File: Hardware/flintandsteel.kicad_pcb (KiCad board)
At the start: 4 copper layers, 57 x 53 mm, 118 parts, among them J1 Conn_01x02_Male, J10 Conn_01x02_Male, J11 Conn_Coaxial, J2 Conn_01x02_Male, J3 Conn_01x02_Male, J4 Conn_01x02_Male, J5 Conn_01x02_Male, J6 Conn_01x02_Male, J7 RBUS, J8 USB_C_Receptacle_USB2.0, J9 Conn_01x02_Male, Q1 MMDT2222A, Q51 PMV20ENR, Q52 PMV20ENR, Q53 PMV20ENR, Q54 PMV20ENR, Q55 PMV20ENR, Q56 PMV20ENR, U1 LTV-247, U2 LTC4411, U3 SC4216H, U4 LTC4411, U5 SN65HVD230, U6 CP2102-GMR-QFN28

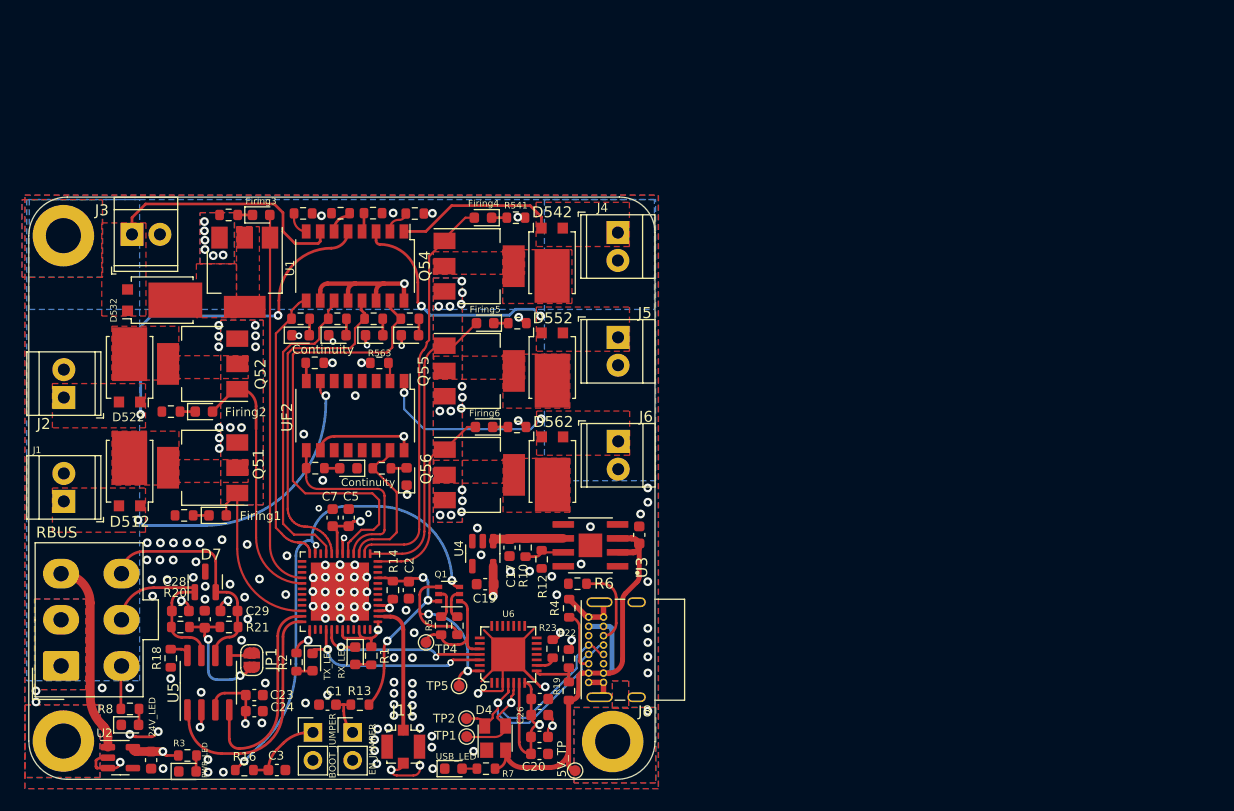
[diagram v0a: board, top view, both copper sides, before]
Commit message: schematic done? + footprints assigned
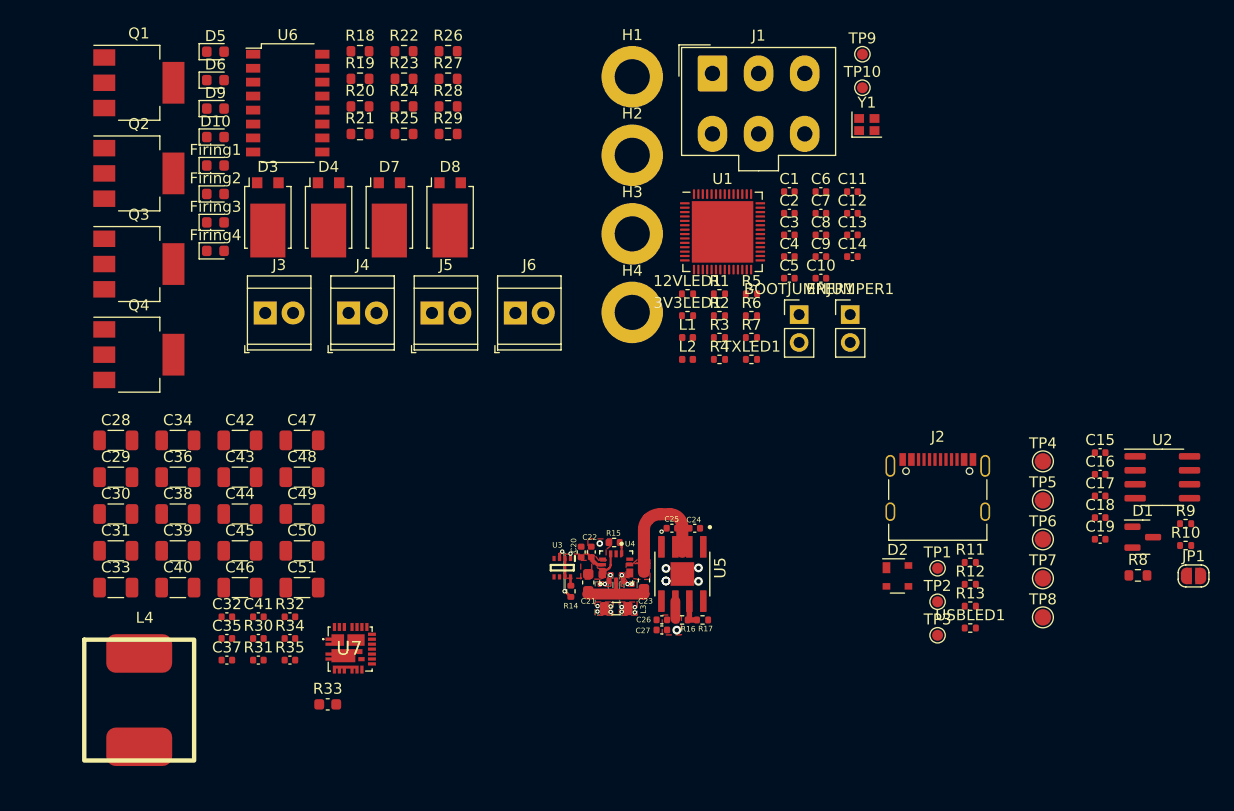
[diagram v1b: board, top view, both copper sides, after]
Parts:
- removed D512, D522, D532, D542, D552, D562: D_Schottky, Package_TO_SOT_SMD:TO-277B
- removed D513, D523, D533, D543, D553, D563: Continuity, LED_SMD:LED_0603_1608Metric
- removed Firing5: D551, LED_SMD:LED_0603_1608Metric
- removed Firing6: D561, LED_SMD:LED_0603_1608Metric
- removed G***: LOGO, iclr:iclr_logo
- removed G***: LOGO, LOGO
- removed GND1: ESP32-PICO-D4, Package_DFN_QFN:QFN-48-1EP_7x7mm_P0.5mm_EP5.3x5.3mm
- removed J10, J9: Conn_01x02_Male, Connector_PinHeader_2.54mm:PinHeader_1x02_P2.54mm_Vertical
- removed J11: Conn_Coaxial, Connector_Coaxial:U.FL_Molex_MCRF_73412-0110_Vertical
- removed J7: RBUS, Connector_Molex:Molex_Mini-Fit_Jr_5566-06A_2x03_P4.20mm_Vertical
- removed J8: USB_C_Receptacle_USB2.0, Connector_USB:USB_C_Receptacle_GCT_USB4085
- removed Q51, Q52, Q53, Q54, Q55, Q56: PMV20ENR, Package_TO_SOT_SMD:SOT-223
- removed R511, R512, R521, R522, R531, R532, R541, R542, R551, R552, R561, R562: 120, Resistor_SMD:R_0603_1608Metric
- removed R513, R523, R533, R543, R553, R563: 10k, Resistor_SMD:R_0603_1608Metric
- removed UF2: LTV-247, Package_SO:SOP-16_4.4x10.4mm_P1.27mm
- added 12VLED1: 12V_LED, Resistor_SMD:R_0402_1005Metric, F.Cu at (178.1, 78.3)
- added 3V3LED1: 3V3LED, Resistor_SMD:R_0402_1005Metric, F.Cu at (178.1, 80.3)
- added BOOTJUMPER1: Conn_01x02_Male, Connector_PinHeader_2.54mm:PinHeader_1x02_P2.54mm_Vertical, F.Cu at (188.3, 80.2)
- added C10: 0.1uF, Capacitor_SMD:C_0402_1005Metric, F.Cu at (190.3, 76.9)
- added C11: 0.1uF, Capacitor_SMD:C_0402_1005Metric, F.Cu at (193.1, 69.0)
- added C12: 4.2pF, Capacitor_SMD:C_0402_1005Metric, F.Cu at (193.1, 71.0)
- added C13: C, Capacitor_SMD:C_0402_1005Metric, F.Cu at (193.1, 72.9)
- added C14: C, Capacitor_SMD:C_0402_1005Metric, F.Cu at (193.1, 74.9)
- added C15: 100nF, Capacitor_SMD:C_0402_1005Metric, F.Cu at (215.7, 92.7)
- added C16: 10uF, Capacitor_SMD:C_0402_1005Metric, F.Cu at (215.7, 94.7)
- added C18: 220pF, Capacitor_SMD:C_0402_1005Metric, F.Cu at (215.7, 98.7)
- added C21: 10uF, Capacitor_SMD:C_0603_1608Metric, F.Cu at (169.1, 104.6)
- added C30: 47uF, Capacitor_SMD:C_1206_3216Metric, F.Cu at (126.1, 98.3)
- added C31: 47uF, Capacitor_SMD:C_1206_3216Metric, F.Cu at (126.1, 101.7)
- added C32: 1uF, Capacitor_SMD:C_0402_1005Metric, F.Cu at (136.2, 107.7)
- added C33: 47uF, Capacitor_SMD:C_1206_3216Metric, F.Cu at (126.1, 105.0)
- added C34: 47uF, Capacitor_SMD:C_1206_3216Metric, F.Cu at (131.7, 91.6)
- added C35: 4.7uF, Capacitor_SMD:C_0402_1005Metric, F.Cu at (136.2, 109.7)
- added C36: 47uF, Capacitor_SMD:C_1206_3216Metric, F.Cu at (131.7, 95.0)
- added C37: 100nF, Capacitor_SMD:C_0402_1005Metric, F.Cu at (136.2, 111.6)
- added C38: 47uF, Capacitor_SMD:C_1206_3216Metric, F.Cu at (131.7, 98.3)
- added C39: 47uF, Capacitor_SMD:C_1206_3216Metric, F.Cu at (131.7, 101.7)
- added C40: 47uF, Capacitor_SMD:C_1206_3216Metric, F.Cu at (131.7, 105.0)
- added C41: 0.1uF, Capacitor_SMD:C_0402_1005Metric, F.Cu at (139.1, 107.7)
- added C42: DNP, Capacitor_SMD:C_1206_3216Metric, F.Cu at (137.4, 91.6)
- added C43: DNP, Capacitor_SMD:C_1206_3216Metric, F.Cu at (137.4, 95.0)
- added C44: DNP, Capacitor_SMD:C_1206_3216Metric, F.Cu at (137.4, 98.3)
- added C45: DNP, Capacitor_SMD:C_1206_3216Metric, F.Cu at (137.4, 101.7)
- added C46: DNP, Capacitor_SMD:C_1206_3216Metric, F.Cu at (137.4, 105.0)
- added C47: DNP, Capacitor_SMD:C_1206_3216Metric, F.Cu at (143.0, 91.6)
- added C48: DNP, Capacitor_SMD:C_1206_3216Metric, F.Cu at (143.0, 95.0)
- added C49: DNP, Capacitor_SMD:C_1206_3216Metric, F.Cu at (143.0, 98.3)
- added C50: DNP, Capacitor_SMD:C_1206_3216Metric, F.Cu at (143.0, 101.7)
- added C51: DNP, Capacitor_SMD:C_1206_3216Metric, F.Cu at (143.0, 105.0)
- added C8: 0.1uF, Capacitor_SMD:C_0402_1005Metric, F.Cu at (190.3, 72.9)
- added C9: 10nF, Capacitor_SMD:C_0402_1005Metric, F.Cu at (190.3, 74.9)
- added D10: Continuity, LED_SMD:LED_0603_1608Metric, F.Cu at (135.2, 64.0)
- added D8: DST1550S, Package_TO_SOT_SMD:TO-277B, F.Cu at (156.5, 71.3)
- added D9: Continuity, LED_SMD:LED_0603_1608Metric, F.Cu at (135.2, 61.4)
- added ENJUMPER1: Conn_01x02_Male, Connector_PinHeader_2.54mm:PinHeader_1x02_P2.54mm_Vertical, F.Cu at (192.9, 80.2)
- added H4: MountingHole_Pad, MountingHole:MountingHole_3.2mm_M3_DIN965_Pad, F.Cu at (173.1, 80.0)
- added L1: 2.0nH, Inductor_SMD:L_0402_1005Metric, F.Cu at (178.1, 82.3)
- added L2: 20nH, Inductor_SMD:L_0402_1005Metric, F.Cu at (178.1, 84.2)
- added L3: 1uH, Inductor_SMD:L_0805_2012Metric, F.Cu at (171.6, 106.9)
- added L4: 680nH, iclr:MGAH1004R68M-10, F.Cu at (123.2, 109.8)
- added Q2: NCV8403, Package_TO_SOT_SMD:SOT-223, F.Cu at (128.2, 67.3)
- added Q3: NCV8403, Package_TO_SOT_SMD:SOT-223, F.Cu at (128.2, 75.6)
- added Q4: NCV8403, Package_TO_SOT_SMD:SOT-223, F.Cu at (128.2, 83.8)
- added R15: 14k, Resistor_SMD:R_0402_1005Metric, F.Cu at (171.4, 100.9)
- added R17: 10k, Resistor_SMD:R_0402_1005Metric, F.Cu at (179.5, 108.0)
- added R24: 120, Resistor_SMD:R_0603_1608Metric, F.Cu at (152.3, 61.2)
- added R25: 120, Resistor_SMD:R_0603_1608Metric, F.Cu at (152.3, 63.7)
- added R26: 120, Resistor_SMD:R_0603_1608Metric, F.Cu at (156.3, 56.2)
- added R27: 120, Resistor_SMD:R_0603_1608Metric, F.Cu at (156.3, 58.7)
- added R28: 10k, Resistor_SMD:R_0603_1608Metric, F.Cu at (156.3, 61.2)
- added R29: 10k, Resistor_SMD:R_0603_1608Metric, F.Cu at (156.3, 63.7)
- added R30: 10k, Capacitor_SMD:C_0402_1005Metric, F.Cu at (139.1, 109.7)
- added R31: 190k, Capacitor_SMD:C_0402_1005Metric, F.Cu at (139.1, 111.6)
- added R32: 10k, Capacitor_SMD:C_0402_1005Metric, F.Cu at (141.9, 107.7)
- added R33: 2.2, Capacitor_SMD:C_0603_1608Metric, F.Cu at (145.4, 115.7)
- added R34: 200k, Capacitor_SMD:C_0402_1005Metric, F.Cu at (141.9, 109.7)
- added R35: 100k, Capacitor_SMD:C_0402_1005Metric, F.Cu at (141.9, 111.6)
- added R9: 60, Resistor_SMD:R_0402_1005Metric, F.Cu at (223.5, 99.2)
- added TP10: TestPoint, TestPoint:TestPoint_Pad_D1.0mm, F.Cu at (194.0, 59.5)
- added TP6: TestPoint, TestPoint:TestPoint_Pad_D1.5mm, F.Cu at (210.5, 100.6)
- added TP7: TestPoint, TestPoint:TestPoint_Pad_D1.5mm, F.Cu at (210.5, 104.2)
- added TP8: TestPoint, TestPoint:TestPoint_Pad_D1.5mm, F.Cu at (210.5, 107.7)
- added TP9: TestPoint, TestPoint:TestPoint_Pad_D1.0mm, F.Cu at (194.0, 56.5)
- added TXLED1: TX_LED, Resistor_SMD:R_0402_1005Metric, F.Cu at (183.9, 84.2)
- added U7: SiC431, iclr:SiC437BEDT1GE3, F.Cu at (147.4, 110.6)
- added USBLED1: USB_LED, Resistor_SMD:R_0402_1005Metric, F.Cu at (203.9, 108.7)
- added Y1: 40MHz±10ppm, Crystal:Crystal_SMD_2016-4Pin_2.0x1.6mm, F.Cu at (194.4, 62.9)
- C1: value 1uF -> 10uF; footprint Capacitor_SMD:C_0603_1608Metric -> Capacitor_SMD:C_0402_1005Metric
- C17: value 10uF -> 47nF; footprint Capacitor_SMD:C_0603_1608Metric -> Capacitor_SMD:C_0402_1005Metric
- C19: value 4.7uF -> 220pF; footprint Capacitor_SMD:C_0603_1608Metric -> Capacitor_SMD:C_0402_1005Metric
- C2, C24, C27: footprint Capacitor_SMD:C_0603_1608Metric -> Capacitor_SMD:C_0402_1005Metric
- C20: value 4.7uF -> 10uF; footprint Capacitor_SMD:C_0603_1608Metric -> Capacitor_SMD:C_0402_1005Metric
- C22: value 1.0uF -> 1uF; footprint Capacitor_SMD:C_0603_1608Metric -> Capacitor_SMD:C_0402_1005Metric
- C23: value 0.1uF -> 22uF
- C25: value 0.1uF -> 4.7uF; footprint Capacitor_SMD:C_0603_1608Metric -> Capacitor_SMD:C_0402_1005Metric
- C26: value 0.1uF -> 10uF; footprint Capacitor_SMD:C_0603_1608Metric -> Capacitor_SMD:C_0402_1005Metric
- C28, C29: value 220pF -> 47uF; footprint Capacitor_SMD:C_0603_1608Metric -> Capacitor_SMD:C_1206_3216Metric
- C3: value 1uF -> 0.1uF; footprint Capacitor_SMD:C_0603_1608Metric -> Capacitor_SMD:C_0402_1005Metric
- C4: value 4.7uF -> 1uF; footprint Capacitor_SMD:C_0603_1608Metric -> Capacitor_SMD:C_0402_1005Metric
- C5, C6: value 10uF -> 0.1uF; footprint Capacitor_SMD:C_0603_1608Metric -> Capacitor_SMD:C_0402_1005Metric
- C7: value 0.1uF -> 1uF; footprint Capacitor_SMD:C_0603_1608Metric -> Capacitor_SMD:C_0402_1005Metric
- D1: value RX_LED -> SM712_SOT23; footprint LED_SMD:LED_0603_1608Metric -> Package_TO_SOT_SMD:SOT-23
- D2: value TX_LED -> SP0503BAHT; footprint LED_SMD:LED_0603_1608Metric -> Package_TO_SOT_SMD:SOT-143
- D3: value PWR_LED -> DST1550S; footprint LED_SMD:LED_0603_1608Metric -> Package_TO_SOT_SMD:TO-277B
- D4: value SP0503BAHT -> DST1550S; footprint Package_TO_SOT_SMD:SOT-143 -> Package_TO_SOT_SMD:TO-277B
- D5: value 24V_LED -> Continuity
- D6: value USB_LED -> Continuity
- D7: value SM712_SOT23 -> DST1550S; footprint Package_TO_SOT_SMD:SOT-23 -> Package_TO_SOT_SMD:TO-277B
- Firing2: value D521 -> D531
- Firing3: value D531 -> D521
- J1: value Conn_01x02_Male -> RBUS; footprint TerminalBlock_TE-Connectivity:TerminalBlock_TE_282834-2_1x02_P2.54mm_Horizontal -> Connector_Molex:Molex_Mini-Fit_Jr_5566-06A_2x03_P4.20mm_Vertical
- J2: value Conn_01x02_Male -> USB_C_Receptacle_USB2.0; footprint TerminalBlock_TE-Connectivity:TerminalBlock_TE_282834-2_1x02_P2.54mm_Horizontal -> Connector_USB:USB_C_Receptacle_Palconn_UTC16-G
- JP1: value SolderJumper_2_Open -> TermJP
- Q1: value MMDT2222A -> NCV8403; footprint Package_TO_SOT_SMD:SOT-363_SC-70-6 -> Package_TO_SOT_SMD:SOT-223
- R1, R3: value 470 -> 10K; footprint Resistor_SMD:R_0603_1608Metric -> Resistor_SMD:R_0402_1005Metric
- R10: value 56k -> 60; footprint Resistor_SMD:R_0603_1608Metric -> Resistor_SMD:R_0402_1005Metric
- R11, R12: value 10K -> 5.1k; footprint Resistor_SMD:R_0603_1608Metric -> Resistor_SMD:R_0402_1005Metric
- R13, R2: footprint Resistor_SMD:R_0603_1608Metric -> Resistor_SMD:R_0402_1005Metric
- R14: value 10K -> 10k; footprint Resistor_SMD:R_0603_1608Metric -> Resistor_SMD:R_0402_1005Metric
- R16: value 470 -> 56k; footprint Resistor_SMD:R_0603_1608Metric -> Resistor_SMD:R_0402_1005Metric
- R18: value 10k -> 120
- R19: value 24k -> 120
- R20, R21: value 60 -> 120
- R22: value 47k -> 10k
- R23: value 4.7k -> 10k
- R4: value 5.1k -> 470; footprint Resistor_SMD:R_0603_1608Metric -> Resistor_SMD:R_0402_1005Metric
- R5: value 10K -> 47.5; footprint Resistor_SMD:R_0603_1608Metric -> Resistor_SMD:R_0402_1005Metric
- R6: value 5.1k -> 499; footprint Resistor_SMD:R_0603_1608Metric -> Resistor_SMD:R_0402_1005Metric
- R7: value 470 -> 3k; footprint Resistor_SMD:R_0603_1608Metric -> Resistor_SMD:R_0402_1005Metric
- R8: value 3k -> 0
- TP4, TP5: footprint TestPoint:TestPoint_Pad_D1.0mm -> TestPoint:TestPoint_Pad_D1.5mm
- U1: value LTV-247 -> ESP32-S3; footprint Package_SO:SOP-16_4.4x10.4mm_P1.27mm -> Package_DFN_QFN:QFN-56-1EP_7x7mm_P0.4mm_EP5.6x5.6mm
- U2: value LTC4411 -> SN65HVD230; footprint Package_TO_SOT_SMD:SOT-23-5 -> Package_SO:SOIC-8_3.9x4.9mm_P1.27mm
- U3: value SC4216H -> LM66200DRLR; footprint iclr:SOIC127P599X175-9N -> iclr:SOTFL50P160X60-8N
- U4: value LTC4411 -> MAX77827AEFD+T; footprint Package_TO_SOT_SMD:SOT-23-5 -> iclr:CONV_MAX77827AEFD+T
- U5: value SN65HVD230 -> SC4215; footprint Package_SO:SOIC-8_3.9x4.9mm_P1.27mm -> iclr:SOIC127P599X175-9N
- U6: value CP2102-GMR-QFN28 -> LTV-247; footprint iclr:QFN28G_0.5-5X5MM -> Package_SO:SOP-16_4.4x10.4mm_P1.27mm
- moved U2 98.2 mm to (221.3, 95.0)
- moved R8 92.6 mm to (219.1, 103.9)
- moved JP1 86.1 mm to (224.2, 104.0), turned to 0 degrees
- moved J2 80.0 mm to (200.9, 95.9), turned to 0 degrees
- moved C4 74.0 mm to (187.4, 74.9), turned to 0 degrees
- moved D1 72.5 mm to (219.6, 100.4), turned to 0 degrees
- moved J1 70.7 mm to (180.4, 58.2), turned to 0 degrees
- moved H3 69.4 mm to (173.1, 72.8)
- moved C3 67.4 mm to (187.4, 72.9)
- moved D6 66.3 mm to (135.2, 58.8)
- moved C1 62.8 mm to (187.4, 69.0), turned to 0 degrees
- moved D5 61.8 mm to (135.2, 56.2)
- moved R3 61.6 mm to (181.0, 82.3), turned to 0 degrees
- moved R10 60.1 mm to (223.5, 101.2), turned to 0 degrees
- moved R19 58.9 mm to (148.3, 58.7), turned to 0 degrees
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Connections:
- C1 pad 1: Net-(C1-Pad1) -> +3V3
- C17 pad 1: GND -> Net-(JP1-B)
- C17 pad 2: Net-(C17-Pad2) -> GND
- C19 pad 1: +3V3 -> GND
- C19 pad 2: GND -> /CAN-
- C2 pad 1: /EN -> /CHIP_PU
- C20 pad 1: GND -> /Power/BBIN
- C20 pad 2: +3V3 -> GND
- C22 pad 1: GND -> /Power/BIAS
- C22 pad 2: +3V3 -> GND
- C23 pad 1: +3V3 -> /Power/BBOUT
- C24 pad 1: +3V3 -> /Power/BBOUT
- C25 pad 1: GND -> /Power/BBOUT
- C25 pad 2: +3V3 -> GND
- C27 pad 1: /Vref -> GND
- C27 pad 2: GND -> +3V3
- C28 pad 1: GND -> /DeployV
- C28 pad 2: /CAN_HIGH -> GND
- C29 pad 1: GND -> /DeployV
- C29 pad 2: /CAN_LOW -> GND
- C3 pad 1: Net-(C3-Pad1) -> /CHIP_PU
- C6 pad 1: GND -> Net-(C6-Pad1)
- C6 pad 2: VBUS -> GND
- D1 pad 1: /RXD -> /CAN-
- D1 pad 2: Net-(D1-Pad2) -> /CAN+
- D2 pad 1: /TXD -> GND
- D2 pad 2: Net-(D2-Pad2) -> VBUS
- D3 pad 1: GND -> Net-(J3-Pin_1)
- D3 pad 2: Net-(D3-Pad2) -> Net-(J3-Pin_1)
- D4 pad 1: GND -> Net-(J4-Pin_1)
- D4 pad 2: VBUS -> Net-(J4-Pin_1)
- D4 pad 3: /Data- -> Net-(D4-K)
- D5 pad 2: Net-(D5-Pad2) -> Net-(D5-A)
- D6 pad 2: Net-(D6-Pad2) -> Net-(D6-A)
- D7 pad 1: /CAN_HIGH -> Net-(J5-Pin_1)
- D7 pad 2: /CAN_LOW -> Net-(J5-Pin_1)
- D7 pad 3: GND -> Net-(D7-K)
- Firing1 pad 1: Net-(Firing1-Pad1) -> Net-(Firing1-K)
- Firing2 pad 1: Net-(R521-Pad1) -> Net-(Firing2-K)
- Firing2 pad 2: /Nuke 2 -> /Nuke 3
- Firing3 pad 2: /Nuke 3 -> /Nuke 2
- J1 pad 1: Net-(D512-Pad1) -> GND
- J1 pad 2: +24V -> GND
- J3 pad 1: Net-(D532-Pad1) -> Net-(J3-Pin_1)
- J3 pad 2: +24V -> +12V
- J4 pad 1: Net-(D542-Pad1) -> Net-(J4-Pin_1)
- J4 pad 2: +24V -> +12V
- J5 pad 1: Net-(D552-Pad1) -> Net-(J5-Pin_1)
- J5 pad 2: +24V -> +12V
- J6 pad 1: Net-(D562-Pad1) -> Net-(J6-Pin_1)
- J6 pad 2: +24V -> +12V
- JP1 pad 1: /Vref -> /CAN-BUS/Vref
- JP1 pad 2: Net-(JP1-Pad2) -> Net-(JP1-B)
- Q1 pad 1: /RTS -> /Nuke 1
- Q1 pad 2: Net-(Q1-Pad2) -> Net-(D3-K)
- Q1 pad 3: /BOOT -> GND
- Q1 pad 4: /DTR -> Net-(D3-K)
- R1 pad 2: Net-(D1-Pad2) -> /CHIP_PU
- R10 pad 1: Net-(C17-Pad2) -> Net-(JP1-B)
- R10 pad 2: Net-(R10-Pad2) -> /CAN-
- R11 pad 1: Net-(Q1-Pad2) -> Net-(J2-CC1)
- R11 pad 2: /DTR -> GND
- R12 pad 1: Net-(R10-Pad2) -> GND
- R12 pad 2: GND -> Net-(J2-CC2)
- R13 pad 1: /EN -> VBUS
- R13 pad 2: Net-(C1-Pad1) -> Net-(USBLED1-A)
- R14 pad 1: +3V3 -> VBUS
- R14 pad 2: /EN -> Net-(U3-ST)
- R16 pad 1: /BOOT -> +3V3
- R16 pad 2: Net-(C3-Pad1) -> /Power/FBIn
- R18 pad 1: Net-(R18-Pad1) -> Net-(Firing1-K)
- R19 pad 1: VBUS -> Net-(Firing2-K)
- R19 pad 2: Net-(R19-Pad2) -> GND
- R2 pad 2: Net-(D2-Pad2) -> Net-(TXLED1-A)
- R20 pad 1: /CAN_HIGH -> /Cont 1
- R20 pad 2: /Vref -> Net-(D5-A)
- R21 pad 1: /Vref -> /Cont 3
- R21 pad 2: /CAN_LOW -> Net-(D6-A)
- R22 pad 1: GND -> Net-(R22-Pad1)
- R22 pad 2: Net-(R19-Pad2) -> GND
- R23 pad 1: +3V3 -> Net-(R23-Pad1)
- R23 pad 2: Net-(R23-Pad2) -> GND
- R3 pad 1: Net-(D3-Pad2) -> +3V3
- R3 pad 2: +3V3 -> /BOOT
- R4 pad 2: GND -> +3V3
- R5 pad 1: Net-(Q1-Pad5) -> GND
- R5 pad 2: /RTS -> Net-(C12-Pad1)
- R6 pad 1: GND -> /TXD
- R6 pad 2: Net-(J8-PadB5) -> Net-(U1-U0TXD/PROG/GPIO43)
- R7 pad 1: VBUS -> +12V
- R7 pad 2: Net-(D6-Pad2) -> Net-(12VLED1-A)
- R8 pad 1: +24V -> Net-(U2-Rs)
- R8 pad 2: Net-(D5-Pad2) -> GND
- TP4 pad 1: /RTS -> /Power/BBIN
- TP5 pad 1: /DTR -> RBUS_uC_V
- U1 pad 1: Net-(D542-Pad1) -> Net-(U1-LNA_IN/RF)
- U1 pad 10: +3V3 -> unconnected-(U1-GPIO5/ADC1_CH4-Pad10)
- U1 pad 11: /Cont 2 -> unconnected-(U1-GPIO6/ADC1_CH5-Pad11)
- U1 pad 12: +3V3 -> unconnected-(U1-GPIO7/ADC1_CH6-Pad12)
- U1 pad 13: /Cont 5 -> unconnected-(U1-GPIO8/ADC1_CH7-Pad13)
- U1 pad 14: +3V3 -> unconnected-(U1-GPIO9/ADC1_CH8-Pad14)
- U1 pad 15: /Cont 4 -> unconnected-(U1-GPIO10/ADC1_CH9-Pad15)
- U1 pad 16: +3V3 -> unconnected-(U1-GPIO11/ADC2_CH0-Pad16)
- U1 pad 2: Net-(R543-Pad1) -> Net-(C6-Pad1)
- U1 pad 3: Net-(D552-Pad1) -> Net-(C6-Pad1)
- U1 pad 4: Net-(R553-Pad1) -> /CHIP_PU
- U1 pad 5: Net-(D522-Pad1) -> /BOOT
- U1 pad 6: Net-(R523-Pad1) -> unconnected-(U1-GPIO1/ADC1_CH0-Pad6)
- U1 pad 7: Net-(D532-Pad1) -> unconnected-(U1-GPIO2/ADC1_CH1-Pad7)
- U1 pad 8: Net-(R533-Pad1) -> unconnected-(U1-GPIO3/ADC1_CH2-Pad8)
- U1 pad 9: /Cont 3 -> unconnected-(U1-GPIO4/ADC1_CH3-Pad9)
- U2 pad 1: Net-(J7-Pad3) -> /CAN_TX
- U2 pad 3: GND -> +3V3
- U2 pad 4: unconnected-(U2-Pad4) -> /CAN_RX
- U2 pad 5: +3V3 -> /CAN-BUS/Vref
- U3 pad 1: unconnected-(U3-Pad1) -> GND
- U3 pad 2: VBUS -> /Power/BBIN
- U3 pad 4: unconnected-(U3-Pad4) -> GND
- U3 pad 5: (no net) -> GND
- U3 pad 6: Net-(C17-Pad2) -> RBUS_uC_V
- U3 pad 7: Net-(R10-Pad2) -> /Power/BBIN
- U3 pad 8: GND -> Net-(U3-ST)
- U4 pad 1: Net-(C17-Pad2) -> /Power/SEL
- U4 pad 2: GND -> unconnected-(U4-POK-Pad2)
- U4 pad 3: GND -> /Power/BBIN
- U4 pad 4: unconnected-(U4-Pad4) -> GND
- U4 pad 5: +3V3 -> /Power/BIAS
- U5 pad 1: /CAN_TX -> unconnected-(U5-PGOOD-Pad1)
- U5 pad 2: GND -> /Power/BBOUT
- U5 pad 3: +3V3 -> /Power/BBOUT
- U5 pad 4: /CAN_RX -> unconnected-(U5-VDD-Pad4)
- U5 pad 5: Net-(JP1-Pad2) -> (no net)
- U5 pad 6: /CAN_LOW -> +3V3
- U5 pad 7: /CAN_HIGH -> /Power/FBIn
- U5 pad 8: Net-(R18-Pad1) -> GND
- U6 pad 1: unconnected-(U6-Pad1) -> Net-(J6-Pin_1)
- U6 pad 10: unconnected-(U6-Pad10) -> +3V3
- U6 pad 11: unconnected-(U6-Pad11) -> /Cont 2
- U6 pad 12: unconnected-(U6-Pad12) -> +3V3
- U6 pad 13: unconnected-(U6-Pad13) -> /Cont 1
- U6 pad 14: unconnected-(U6-Pad14) -> +3V3
- U6 pad 15: unconnected-(U6-Pad15) -> /Cont 4
- U6 pad 16: unconnected-(U6-Pad16) -> +3V3
- U6 pad 2: unconnected-(U6-Pad2) -> Net-(R29-Pad1)
- U6 pad 3: GND -> Net-(J3-Pin_1)
- U6 pad 4: /Data+ -> Net-(R22-Pad1)
- U6 pad 5: /Data- -> Net-(J5-Pin_1)
- U6 pad 6: +3V3 -> Net-(R28-Pad1)
- U6 pad 7: +3V3 -> Net-(J4-Pin_1)
- U6 pad 8: Net-(R19-Pad2) -> Net-(R23-Pad1)
- U6 pad 9: Net-(R23-Pad2) -> /Cont 3
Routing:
- net +3V3: track 70.1 -> 1.61 mm, vias 11 -> 1
- net GND: track 53.7 -> 6.73 mm, vias 161 -> 8
- net /BOOT: track 43.9 -> 0.00 mm, vias 3 -> 0
- net /Cont 4: track 41.1 -> 0.00 mm
- net VBUS: track 45.6 -> 5.27 mm, vias 0 -> 2
- net /Nuke 4: track 36.6 -> 0.00 mm
- net /Nuke 3: track 34.5 -> 0.00 mm
- net Net-(D522-Pad1): track 31.9 -> 0.00 mm, vias 2 -> 0
- net /Cont 5: track 31.0 -> 0.00 mm
- net /Cont 2: track 28.9 -> 0.00 mm
- net /Nuke 5: track 26.8 -> 0.00 mm
- net /Cont 3: track 26.0 -> 0.00 mm
- net Net-(D512-Pad1): track 25.5 -> 0.00 mm, vias 2 -> 0
- net /Nuke 2: track 23.5 -> 0.00 mm
- net /Data-: track 23.0 -> 0.00 mm, vias 1 -> 0
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- added copper zone on F.Cu, net +3V3
- added copper zone on F.Cu, net /Power/BBIN
- added copper zone on F.Cu, net /Power/BBOUT
- added copper zone on B.Cu, net /Power/LX1
- added copper zone on F.Cu, net /Power/LX1
- added copper zone on B.Cu, net /Power/LX2
- added copper zone on F.Cu, net /Power/LX2
- removed copper zone on B.Cu, net +24V
- removed copper zone on In2.Cu, net +3V3
- removed copper zone on B.Cu, net GND
- removed copper zone on In1.Cu, net GND
- removed copper zone on F.Cu, net Net-(D512-Pad1)
- removed copper zone on F.Cu, net Net-(D512-Pad3)
- removed copper zone on F.Cu, net Net-(D522-Pad1)
- removed copper zone on F.Cu, net Net-(D522-Pad3)
- removed copper zone on F.Cu, net Net-(D532-Pad1)
- removed copper zone on F.Cu, net Net-(D532-Pad3)
- removed copper zone on F.Cu, net Net-(D542-Pad1)
- removed copper zone on F.Cu, net Net-(D542-Pad3)
- removed copper zone on F.Cu, net Net-(D552-Pad1)
- removed copper zone on F.Cu, net Net-(D552-Pad3)
- removed copper zone on F.Cu, net Net-(D562-Pad1)
- removed copper zone on F.Cu, net Net-(D562-Pad3)
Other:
- board outline removed
- board text removed: "5V_TP"
- board text removed: "BOOT_JUMPER"
- board text removed: "Continuity"
- board text removed: "Designed By Jiawei Yao Andrei Paduraru"
- board text removed: "EN_JUMPER"
- board text removed: "FLINT & STEEL v1"

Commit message: started pyro channel layout
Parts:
- added 16VLED1: 16V_LED, Resistor_SMD:R_0402_1005Metric, F.Cu at (185.2, 91.3)
- added R36: 3k, Resistor_SMD:R_0402_1005Metric, F.Cu at (185.2, 93.3)
- moved C25 177.1 mm to (336.3, 23.0)
- moved R17 177.1 mm to (339.1, 31.4)
- moved C21 177.1 mm to (328.7, 28.0)
- moved C22 177.1 mm to (329.0, 25.2)
- moved C23 177.1 mm to (333.8, 27.8)
- moved C24 177.1 mm to (338.4, 23.0)
- moved C26 177.1 mm to (335.4, 31.4)
- moved C27 177.1 mm to (335.4, 32.3)
- moved R14 177.1 mm to (327.1, 28.8)
- moved R16 177.1 mm to (337.3, 31.4)
- moved U3 177.1 mm to (326.4, 26.6)
- moved U4 177.1 mm to (331.3, 26.6)
- moved U5 177.1 mm to (337.3, 27.2)
- moved C20 177.1 mm to (328.1, 25.2)
- moved L3 177.1 mm to (331.3, 30.3)
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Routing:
- added copper zone on F.Cu, net Net-(D3-K)
- added copper zone on F.Cu, net Net-(D4-K)
- added copper zone on F.Cu, net Net-(J3-Pin_1)
- added copper zone on F.Cu, net Net-(J4-Pin_1)

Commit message: pyro channels & tiny buck passives
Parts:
- moved C23 237.5 mm to (133.3, 155.0)
- moved C25 237.5 mm to (135.8, 150.3)
- moved C26 237.5 mm to (134.9, 158.6)
- moved C27 237.5 mm to (134.9, 159.5)
- moved R16 237.5 mm to (136.7, 158.6)
- moved R17 237.5 mm to (138.6, 158.6)
- moved U5 237.5 mm to (136.7, 154.5)
- moved C20 237.5 mm to (127.5, 152.4)
- moved C21 237.5 mm to (128.2, 155.2)
- moved C22 237.5 mm to (128.5, 152.4)
- moved C24 237.5 mm to (137.9, 150.3)
- moved L3 237.5 mm to (130.7, 157.6)
- moved R14 237.5 mm to (126.6, 156.0)
- moved R15 237.5 mm to (130.5, 151.6)
- moved U3 237.5 mm to (125.8, 153.9)
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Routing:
- net /DeployV: track 0.00 -> 7.12 mm
- net /buckC/FB: track 0.00 -> 3.38 mm
- net +12V: track 0.00 -> 2.57 mm
- net /buckC/VDD: track 0.00 -> 2.54 mm, vias 0 -> 1
- net GND: track 6.73 -> 9.22 mm
- net /buckC/PHASE: track 0.00 -> 1.96 mm
- net Net-(U7-V_DRV): track 0.00 -> 1.76 mm
- net Net-(U7-MODE_2): track 0.00 -> 1.62 mm
- net Net-(C41-Pad2): track 0.00 -> 1.53 mm
- net /buckC/BOOT: track 0.00 -> 1.44 mm
- net Net-(U7-_MODE_1): track 0.00 -> 1.42 mm
- added copper zone on F.Cu, net Net-(D7-K)
- added copper zone on F.Cu, net Net-(D8-K)
- added copper zone on F.Cu, net Net-(J5-Pin_1)
- added copper zone on F.Cu, net Net-(J6-Pin_1)
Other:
- rule pad_to_mask_clearance: 0 -> 0.05

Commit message: I had to get back out of bed to push this commit
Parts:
- J1: footprint Connector_Molex:Molex_Mini-Fit_Jr_5566-06A_2x03_P4.20mm_Vertical -> Connector_Molex:Molex_Mini-Fit_Jr_5569-08A2_2x04_P4.20mm_Horizontal
- JP1: footprint Jumper:SolderJumper-2_P1.3mm_Open_RoundedPad1.0x1.5mm -> iclr:SmallerSolderJP
- R10, R9: footprint Resistor_SMD:R_0402_1005Metric -> Resistor_SMD:R_0603_1608Metric
- moved J1 125.1 mm to (55.3, 59.8), turned to 90 degrees
- moved L1 53.2 mm to (224.9, 57.1)
- moved R1 48.0 mm to (225.2, 59.6)
- moved L2 42.4 mm to (214.8, 63.0), turned to -90 degrees
- moved C3 42.3 mm to (227.9, 60.7)
- moved C2 42.1 mm to (227.9, 59.7)
- moved C8 42.0 mm to (230.3, 60.5)
- moved BOOTJUMPER1 41.8 mm to (228.3, 68.2)
- moved ENJUMPER1 41.8 mm to (233.0, 68.2)
- moved R5 39.2 mm to (219.0, 60.6), turned to 90 degrees
- moved C4 39.2 mm to (221.9, 56.4)
- moved C5 39.2 mm to (221.9, 58.4)
- moved C1 37.0 mm to (221.7, 55.0)
- moved C6 37.0 mm to (224.6, 55.0)
- moved C10 34.1 mm to (214.6, 53.0)
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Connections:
- J1 pad 3: RBUS_uC_V -> GND
- J1 pad 4: /DeployV -> RBUS_uC_V
- J1 pad 5: /CAN+ -> /DeployV
- J1 pad 6: /CAN- -> /DeployV
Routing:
- net /CAN+: track 0.00 -> 9.08 mm
- net /CAN-: track 0.00 -> 8.88 mm

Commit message: I don't remember what I did but I have to move these files to my desktop
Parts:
- moved H2 120.6 mm to (60.5, 22.5)
- moved H3 112.6 mm to (60.5, 70.5)
- moved H1 74.0 mm to (108.5, 22.5)
- moved C28 70.8 mm to (151.2, 109.7)
- moved C29 70.8 mm to (151.2, 106.4)
- moved C30 70.8 mm to (151.2, 103.0)
- moved C31 70.8 mm to (151.2, 99.7)
- moved C33 70.8 mm to (151.2, 96.3)
- moved C34 70.8 mm to (151.2, 112.6)
- moved H4 65.3 mm to (108.5, 70.5)
- moved C36 45.3 mm to (88.0, 83.0), turned to 90 degrees
- moved C38 43.2 mm to (91.3, 83.0), turned to 90 degrees
- moved C39 41.5 mm to (94.7, 83.0), turned to 90 degrees
- moved C40 40.2 mm to (98.0, 83.0), turned to 90 degrees
- moved L4 39.2 mm to (81.5, 72.4)
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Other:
- board outline added: 55 x 55 mm

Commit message: High power side nearly done
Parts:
- J3, J4, J5, J6: footprint TerminalBlock_TE-Connectivity:TerminalBlock_TE_282834-2_1x02_P2.54mm_Horizontal -> TerminalBlock_Phoenix:TerminalBlock_Phoenix_PT-1,5-2-3.5-H_1x02_P3.50mm_Horizontal
- moved C45 155.7 mm to (69.2, 66.0), turned to 180 degrees
- moved H4 110.1 mm to (207.0, 21.2)
- moved C30 82.0 mm to (87.5, 60.9)
- moved C31 79.0 mm to (87.5, 56.3)
- moved C34 78.4 mm to (87.5, 54.0)
- moved C28 77.5 mm to (87.6, 65.5)
- moved C29 76.9 mm to (87.5, 63.2)
- moved C33 74.0 mm to (87.5, 58.6)
- moved J1 65.3 mm to (104.4, 46.5), turned to -90 degrees
- moved J6 56.8 mm to (61.9, 28.9)
- moved J3 53.8 mm to (61.9, 57.2)
- moved H1 53.1 mm to (98.5, 74.6)
- moved H2 52.0 mm to (60.5, 74.5)
- moved D8 48.0 mm to (67.8, 30.9), turned to 180 degrees
- moved J5 47.8 mm to (61.9, 38.3)
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- renumbered C34 to C30, C30 to C31, C31 to C34
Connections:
- net Net-(U7-MODE_2) renamed /buckC/MODE2
- D3 pad 1: Net-(J3-Pin_1) -> Net-(J3-Pin_2)
- D3 pad 2: Net-(J3-Pin_1) -> Net-(J3-Pin_2)
- D4 pad 1: Net-(J4-Pin_1) -> Net-(J4-Pin_2)
- D4 pad 2: Net-(J4-Pin_1) -> Net-(J4-Pin_2)
- D7 pad 1: Net-(J5-Pin_1) -> Net-(J5-Pin_2)
- D7 pad 2: Net-(J5-Pin_1) -> Net-(J5-Pin_2)
- D8 pad 1: Net-(J6-Pin_1) -> Net-(J6-Pin_2)
- D8 pad 2: Net-(J6-Pin_1) -> Net-(J6-Pin_2)
- J3 pad 1: Net-(J3-Pin_1) -> +12V
- J3 pad 2: +12V -> Net-(J3-Pin_2)
- J4 pad 1: Net-(J4-Pin_1) -> +12V
- J4 pad 2: +12V -> Net-(J4-Pin_2)
- J5 pad 1: Net-(J5-Pin_1) -> +12V
- J5 pad 2: +12V -> Net-(J5-Pin_2)
- J6 pad 1: Net-(J6-Pin_1) -> +12V
- J6 pad 2: +12V -> Net-(J6-Pin_2)
- U6 pad 1: Net-(J6-Pin_1) -> Net-(J6-Pin_2)
- U6 pad 3: Net-(J3-Pin_1) -> Net-(J3-Pin_2)
- U6 pad 5: Net-(J5-Pin_1) -> Net-(J5-Pin_2)
- U6 pad 7: Net-(J4-Pin_1) -> Net-(J4-Pin_2)
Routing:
- net +12V: vias 0 -> 15
- net GND: vias 8 -> 14
- added copper zone on B.Cu, net +12V
- added copper zone on F.Cu, net +12V
- added copper zone on F.Cu, net /buckC/SW
- added copper zone on F.Cu, net Net-(J3-Pin_2)
- added copper zone on F.Cu, net Net-(J4-Pin_2)
- added copper zone on F.Cu, net Net-(J5-Pin_2)
- added copper zone on F.Cu, net Net-(J6-Pin_2)
- removed copper zone on F.Cu, net Net-(J3-Pin_1)
- removed copper zone on F.Cu, net Net-(J4-Pin_1)
- removed copper zone on F.Cu, net Net-(J5-Pin_1)
- removed copper zone on F.Cu, net Net-(J6-Pin_1)
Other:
- board size 55 x 55 mm -> 44 x 57 mm

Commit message: high V side finished, CAN circuit and ESP left to place
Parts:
- removed the C29 at (87.5, 63.2)
- removed C51: DNP, Capacitor_SMD:C_1206_3216Metric
- 12VLED1, 16VLED1, 3V3LED1: footprint Resistor_SMD:R_0402_1005Metric -> Diode_SMD:D_0402_1005Metric
- C42, C44, C46, C48, C50: moved to B.Cu
- U1: footprint Package_DFN_QFN:QFN-56-1EP_7x7mm_P0.4mm_EP5.6x5.6mm -> iclr:QFN40P700X700X90-57N
- moved D1 228.5 mm to (12.5, 88.0), turned to 0 degrees
- moved C18 227.3 mm to (14.9, 89.4), turned to -90 degrees
- moved R9 226.6 mm to (16.1, 89.9), turned to 90 degrees
- moved C17 225.5 mm to (15.4, 88.0), turned to 180 degrees
- moved R8 225.2 mm to (18.9, 91.5), turned to 0 degrees
- moved C19 224.7 mm to (14.9, 86.6), turned to 90 degrees
- moved R10 222.9 mm to (16.1, 86.0), turned to 90 degrees
- moved U2 219.6 mm to (21.1, 88.1), turned to 180 degrees
- moved JP1 219.3 mm to (18.3, 84.7), turned to 180 degrees
- moved C15 215.4 mm to (25.2, 88.1), turned to -90 degrees
- moved C16 214.4 mm to (26.2, 88.1), turned to -90 degrees
- moved ENJUMPER1 186.2 mm to (48.2, 90.9)
- moved BOOTJUMPER1 185.1 mm to (44.6, 91.0)
- moved C42 151.8 mm to (44.6, 117.0), turned to -90 degrees
- moved C48 151.3 mm to (51.5, 117.0), turned to -90 degrees
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- renumbered C33 to C29, C34 to C31, C31 to C33, R29 to R22, R22 to R23, R23 to R29
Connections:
- D2 pad 2: VBUS -> /Data-
- D2 pad 3: /Data- -> /Data+
- D2 pad 4: /Data+ -> VBUS
- R36 pad 1: +12V -> /DeployV
- U6 pad 1: Net-(J6-Pin_2) -> Net-(J3-Pin_2)
- U6 pad 13: /Cont 1 -> /Cont 3
- U6 pad 15: /Cont 4 -> /Cont 1
- U6 pad 3: Net-(J3-Pin_2) -> Net-(J4-Pin_2)
- U6 pad 7: Net-(J4-Pin_2) -> Net-(J6-Pin_2)
- U6 pad 9: /Cont 3 -> /Cont 4
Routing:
- net Net-(J6-Pin_2): track 0.00 -> 48.5 mm
- net Net-(J5-Pin_2): track 0.00 -> 37.3 mm
- net Net-(J4-Pin_2): track 0.00 -> 26.0 mm
- net +12V: track 2.57 -> 19.8 mm
- net /DeployV: track 7.12 -> 19.5 mm, vias 0 -> 10
- net +3V3: track 1.61 -> 10.4 mm, vias 1 -> 5
- net Net-(U1-XTAL_N): track 0.00 -> 7.54 mm
- net GND: track 9.22 -> 15.7 mm, vias 14 -> 138
- net /buckC/VDD: track 2.54 -> 7.36 mm, vias 1 -> 2
- net Net-(J3-Pin_2): track 0.00 -> 4.23 mm
- net Net-(C14-Pad1): track 0.00 -> 2.57 mm
- net Net-(R22-Pad1): track 0.00 -> 2.28 mm
- net Net-(R28-Pad1): track 0.00 -> 1.84 mm
- net /Power/BBOUT: track 12.3 -> 10.5 mm
- net Net-(R29-Pad1): track 0.00 -> 1.62 mm
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- added copper zone on B.Cu, net /DeployV
- added copper zone on F.Cu, net /DeployV
- added copper zone on B.Cu, net GND
- added copper zone on In1.Cu, net GND
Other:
- board size 44 x 57 mm -> 44 x 62.9 mm
